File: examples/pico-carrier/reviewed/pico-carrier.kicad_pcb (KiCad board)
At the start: 2 copper layers, 88 x 62 mm, 9 parts, among them J1 5V IN, J3 GP0-GP15, J4 GP16-GP28, PWR, U1 Pico

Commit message: Keep vias out of the lands they would drain
The reviewer's next one, and it is not one board's problem: vias were
landing inside surface-mount lands across the set. A hole in a land is a
hole solder wicks down during reflow - the joint above it starves, and
nothing on the assembled board tells that apart from a cold one.
Via-in-pad is a real technique and a filled-and-capped process, not a
drawing; a layout that has not specified the process may not draw it.

The router was the source. `_blocked` skips a route's own net, so
nothing stopped a layer change from happening on the very land the route
started at, and eighteen vias across three boards sat in one. Pads are
now marked as pads in the obstacle list and every one of them, whoever
owns it, is a cell where a via may not go - so an escape that has to
reach the plane leaves the land first and turns its via beside it. The
stitching pass kept ground vias a via-radius from ground lands where it
kept signal ones a radius plus clearance; both are the same distance
now, because the plane gains nothing from touching a land it can reach a
stub away.

`via.in_pad` measures the copper gap from every via to every land and
reports what is left. The exposed thermal pad under a package is exempt
- the via array in one is the datasheet's own answer, and nothing a
signal reaches is four square millimetres. It blocks under the
ai-generated policy: a generated board has no reason to draw this.

The test fixture had one too, a via twenty-five microns into C1's ground
land; it moves three tenths of a millimetre and the board is DRC clean
on both matrix versions as before.

Co-Authored-By: Claude Fable 5 <noreply@anthropic.com>
Claude-Session: https://claude.ai/code/session_01DUj7Ltu92tWg159mCSacwY
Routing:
- net GND: track 65.7 -> 66.1 mm, vias 56 -> 55
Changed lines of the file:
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@@
 	(segment (start 135.69 94.48) (end 142.0 94.48) (width 0.8) (layer "F.Cu") (net 1))
 	(segment (start 135.69 107.18) (end 142.0 107.18) (width 0.8) (layer "F.Cu") (net 1))
-	(segment (start 152.0 67.045) (end 152.045 67.045) (width 0.5) (layer "F.Cu") (net 1))
-	(segment (start 152.045 67.045) (end 152.25 67.25) (width 0.5) (layer "F.Cu") (net 1))
-	(segment (start 152.25 67.25) (end 153.5 68.5) (width 0.5) (layer "F.Cu") (net 1))
-	(segment (start 153.5 68.5) (end 155.0 70.0) (width 0.5) (layer "B.Cu") (net 1))
-	(segment (start 155.0 70.0) (end 155.0 74.0) (width 0.5) (layer "B.Cu") (net 1))
+	(segment (start 152.0 67.045) (end 152.205 67.045) (width 0.5) (layer "F.Cu") (net 1))
+	(segment (start 152.205 67.045) (end 152.25 67.0) (width 0.5) (layer "F.Cu") (net 1))
+	(segment (start 152.25 67.0) (end 152.75 67.0) (width 0.5) (layer "F.Cu") (net 1))
+	(segment (start 152.75 67.0) (end 154.25 68.5) (width 0.5) (layer "F.Cu") (net 1))
+	(segment (start 154.25 68.5) (end 155.0 69.25) (width 0.5) (layer "B.Cu") (net 1))
+	(segment (start 155.0 69.25) (end 155.0 74.0) (width 0.5) (layer "B.Cu") (net 1))
 	(segment (start 152.95 77.0) (end 154.5 77.0) (width 0.5) (layer "F.Cu") (net 1))
 	(segment (start 170.9375 77.0) (end 171.0 77.0) (width 0.5) (layer "F.Cu") (net 1))
@@
 	(segment (start 159.5 75.5) (end 149.5 75.5) (width 0.4) (layer "F.Cu") (net 2))
 	(segment (start 162.9125 77.0) (end 169.0625 77.0) (width 0.3) (layer "F.Cu") (net 33))
-	(via (at 153.5 68.5) (size 0.8) (drill 0.4) (layers "F.Cu" "B.Cu") (net 1))
+	(via (at 154.25 68.5) (size 0.8) (drill 0.4) (layers "F.Cu" "B.Cu") (net 1))
 	(via (at 154.5 77.0) (size 0.8) (drill 0.4) (layers "F.Cu" "B.Cu") (net 1))
 	(via (at 174.0 81.0) (size 0.8) (drill 0.4) (layers "F.Cu" "B.Cu") (net 1))
@@
 	(via (at 102.7 112.7) (size 0.8) (drill 0.4) (layers "F.Cu" "B.Cu") (net 1))
 	(via (at 185.3 112.7) (size 0.8) (drill 0.4) (layers "F.Cu" "B.Cu") (net 1))
-	(via (at 108.7 68.7) (size 0.8) (drill 0.4) (layers "F.Cu" "B.Cu") (net 1))
 	(via (at 120.7 68.7) (size 0.8) (drill 0.4) (layers "F.Cu" "B.Cu") (net 1))
 	(via (at 156.7 68.7) (size 0.8) (drill 0.4) (layers "F.Cu" "B.Cu") (net 1))

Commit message: Give the vias room to stand beside the lands
Following the via-in-pad ban, the FPGA board stopped routing: five
attempts, five different nets, each one out of lanes in the corridor
between the FPGA's east escape fan and the codec's west one. Three
changes, in the order a layout would make them.

The via spacing was guesswork and is now the fab's. Hole to hole goes
from 1.2 mm to 0.9, which at the shipped 0.8/0.4 via leaves half a
millimetre of laminate between barrels - the ordinary minimum - and in a
1 mm-pitch escape comb is the difference between a lane and no lane.
What a via keeps off a land it may not sit in is its own radius plus a
solder-mask dam rather than the track clearance: the copper either side
may well be the same net, and what has to be true is that the mask can
part the barrel from the land.

Every decoupling capacitor now has its ground via placed against its own
pad rather than nine of them asking the search for one, and where the
via goes is chosen rather than fixed: `anchor_site` takes the nearest
position that clears everything already placed, fanning either side of
the direction facing off the part. A fixed offset walled off the
corridor its neighbour's supply needed - the via was legal, and it was
in the way.

And the seven parts sitting inside that corridor - four decoupling
capacitors, the two 1.2 V ones and the LED resistor - move four
millimetres south into the empty band below it. Twelve lanes leaving the
FPGA and ten arriving at the codec have eleven millimetres to cross in;
what a hand would do first is stop parking capacitors in the middle of
that, and it is the floorplan half of the debt this board's own README
has been carrying.

Co-Authored-By: Claude Fable 5 <noreply@anthropic.com>
Claude-Session: https://claude.ai/code/session_01DUj7Ltu92tWg159mCSacwY
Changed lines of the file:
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@@
 	(segment (start 135.69 94.48) (end 142.0 94.48) (width 0.8) (layer "F.Cu") (net 1))
 	(segment (start 135.69 107.18) (end 142.0 107.18) (width 0.8) (layer "F.Cu") (net 1))
-	(segment (start 152.0 67.045) (end 152.205 67.045) (width 0.5) (layer "F.Cu") (net 1))
-	(segment (start 152.205 67.045) (end 152.25 67.0) (width 0.5) (layer "F.Cu") (net 1))
-	(segment (start 152.25 67.0) (end 152.75 67.0) (width 0.5) (layer "F.Cu") (net 1))
-	(segment (start 152.75 67.0) (end 154.25 68.5) (width 0.5) (layer "F.Cu") (net 1))
-	(segment (start 154.25 68.5) (end 155.0 69.25) (width 0.5) (layer "B.Cu") (net 1))
-	(segment (start 155.0 69.25) (end 155.0 74.0) (width 0.5) (layer "B.Cu") (net 1))
+	(segment (start 152.0 67.045) (end 152.045 67.045) (width 0.5) (layer "F.Cu") (net 1))
+	(segment (start 152.045 67.045) (end 152.25 67.25) (width 0.5) (layer "F.Cu") (net 1))
+	(segment (start 152.25 67.25) (end 153.5 68.5) (width 0.5) (layer "F.Cu") (net 1))
+	(segment (start 153.5 68.5) (end 155.0 70.0) (width 0.5) (layer "B.Cu") (net 1))
+	(segment (start 155.0 70.0) (end 155.0 74.0) (width 0.5) (layer "B.Cu") (net 1))
 	(segment (start 152.95 77.0) (end 154.5 77.0) (width 0.5) (layer "F.Cu") (net 1))
 	(segment (start 170.9375 77.0) (end 171.0 77.0) (width 0.5) (layer "F.Cu") (net 1))
@@
 	(segment (start 159.5 75.5) (end 149.5 75.5) (width 0.4) (layer "F.Cu") (net 2))
 	(segment (start 162.9125 77.0) (end 169.0625 77.0) (width 0.3) (layer "F.Cu") (net 33))
-	(via (at 154.25 68.5) (size 0.8) (drill 0.4) (layers "F.Cu" "B.Cu") (net 1))
+	(via (at 153.5 68.5) (size 0.8) (drill 0.4) (layers "F.Cu" "B.Cu") (net 1))
 	(via (at 154.5 77.0) (size 0.8) (drill 0.4) (layers "F.Cu" "B.Cu") (net 1))
 	(via (at 174.0 81.0) (size 0.8) (drill 0.4) (layers "F.Cu" "B.Cu") (net 1))

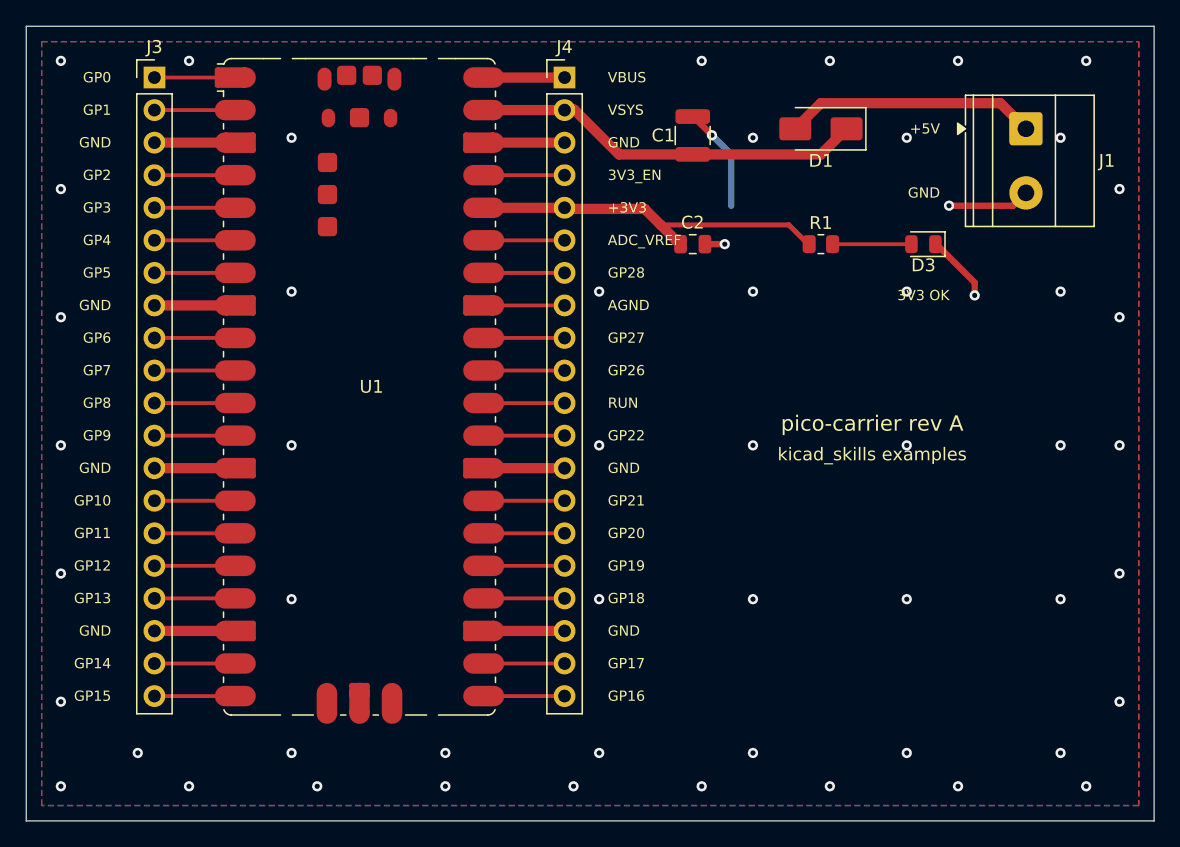
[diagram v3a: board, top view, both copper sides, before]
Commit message: Relieve the pads, fillet the joints, and give the board its screw holes
Three of the reviewer's manufacturing points, and they largely fall out
of the one before it - once KiCad fills the plane, the thermal relief it
was already asked for in the file actually appears.

**Thermal relief.** The zones said thermal all along; our own filler
ignored it and flooded every land solid. KiCad's does not, so every
through-hole ground pad now sits in a gap bridged by four spokes and an
iron can bring the joint up without heating a hundred square millimetres
of copper. `layout.solid_pad_connection` reports the setting when a
board turns it off: drilled pads only, because a surface pad reflows in
an oven that is heating the plane anyway and flooding it is often the
better thermal answer.

**Teardrops.** A track entering a land is a step change in width, and a
step change is where copper tears - the connector gets levered on and
off, the drill wanders, and the crack starts at the corner. `_teardrops`
replaces the first stretch of each run with a three-step taper into the
land, checked against its neighbours before it is kept, so a fillet
never eats the clearance a fine-pitch escape needs. It *replaces* rather
than overlays: laying the taper on top of the run drew the same copper
twice, and `route.acute_angle` reported all thirty of them, correctly.
`route.mixed_track_widths` learns what a fillet looks like so a properly
filleted board does not read as one nobody decided the width of.

**Mounting holes.** Four M3 holes near the corners, placed before the
router runs because they are obstacles, and slid along the edges or a
little inboard where a connector body has the corner - the motor board
and the op-amp take three, which is what those floorplans have room for.
Grounded on the motor driver, whose chassis is metal and part of the
shield, plain on the rest: bonding the enclosure to the reference is the
enclosure's decision, not the board's.

Two things that fell out of placing par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
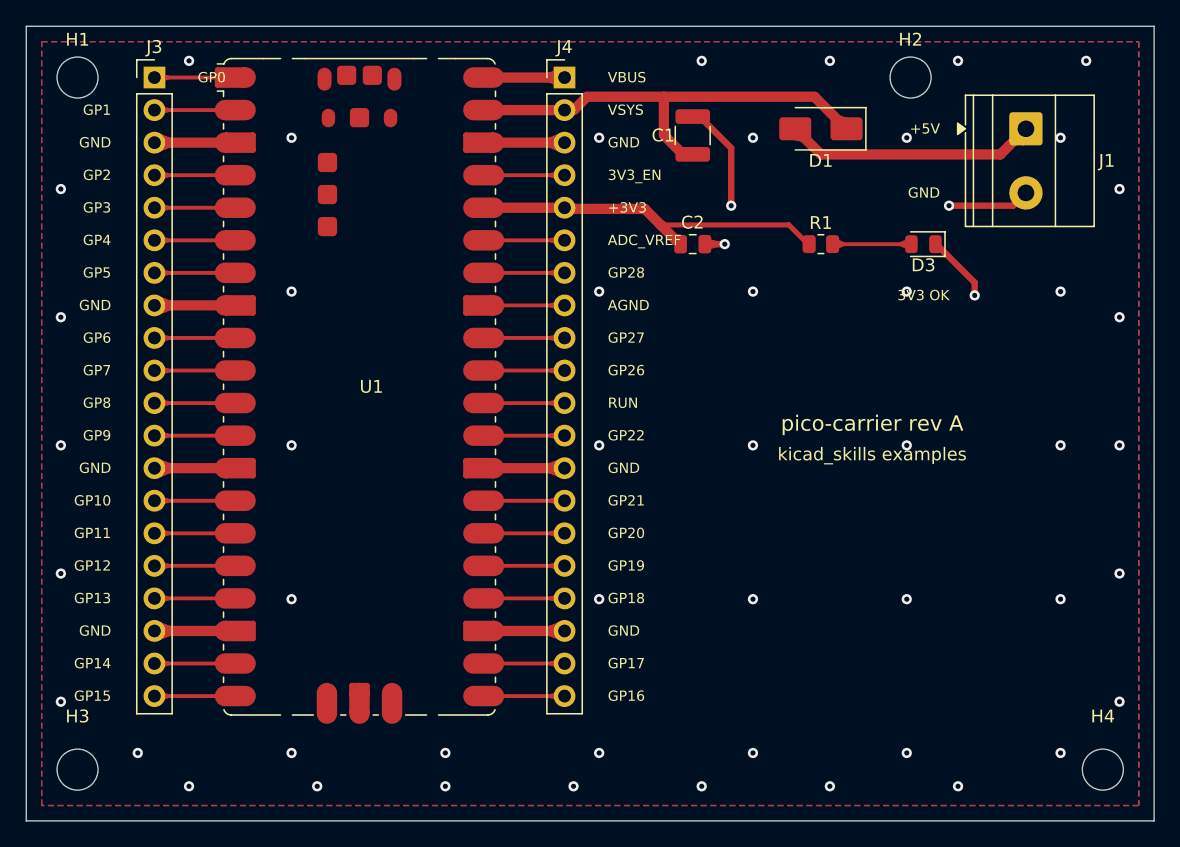
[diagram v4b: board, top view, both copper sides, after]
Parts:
- added H1: M33, MountingHole:MountingHole_3.2mm_M3, F.Cu at (104.0, 64.0)
- added H2: M33, MountingHole:MountingHole_3.2mm_M3, F.Cu at (169.0, 64.0)
- added H3: M33, MountingHole:MountingHole_3.2mm_M3, F.Cu at (104.0, 118.0)
- added H4: M33, MountingHole:MountingHole_3.2mm_M3, F.Cu at (184.0, 118.0)
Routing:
- net /VSYS: track 30.6 -> 35.6 mm
- net GND: track 65.7 -> 66.0 mm, vias 55 -> 53

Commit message: Give the assembly machine something to aim at
Fiducials: three copper dots in bare mask windows, near three different
corners so a pick-and-place gets rotation as well as offset. It aligns
to the board, not to the drawing - without them it has only the routed
outline, cut to a tolerance ten times looser than the placement a 0.5 mm
pitch part is asking for. `fab.no_fiducials` reports a fine-pitch board
that has none, as context rather than as a fault: plenty of boards are
built one at a time with tweezers.

They share the corner search with the mounting holes, which is where
this found a real bug: `_courtyard_box` read lines and rectangles only,
and a mounting hole draws its courtyard as one circle - so every hole
measured as taking up no room at all, and the first three fiducials
landed on top of three screw holes. Circles and arcs count now.

Co-Authored-By: Claude Fable 5 <noreply@anthropic.com>
Claude-Session: https://claude.ai/code/session_01DUj7Ltu92tWg159mCSacwY
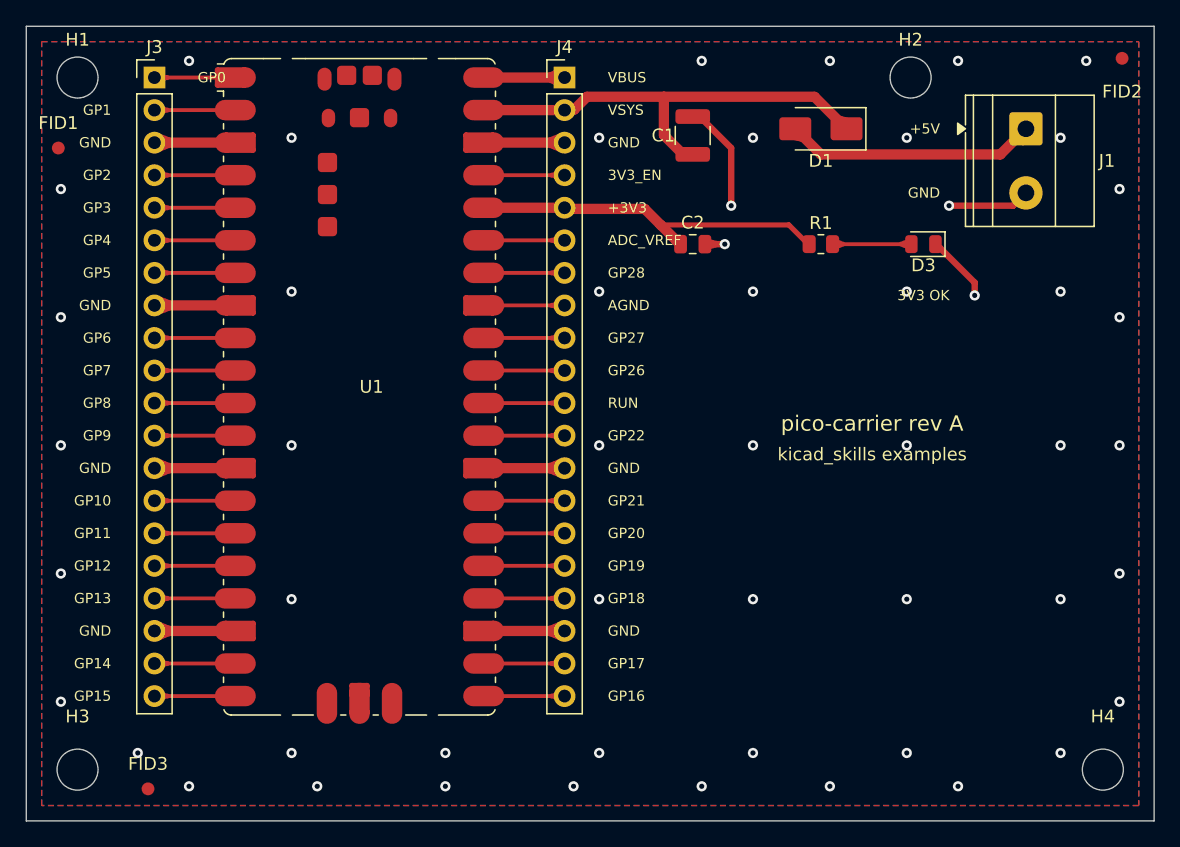
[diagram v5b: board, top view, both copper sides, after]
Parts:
- added FID1: Fiducial, Fiducial:Fiducial_1mm_Mask2mm, F.Cu at (102.5, 69.5)
- added FID2: Fiducial, Fiducial:Fiducial_1mm_Mask2mm, F.Cu at (185.5, 62.5)
- added FID3: Fiducial, Fiducial:Fiducial_1mm_Mask2mm, F.Cu at (109.5, 119.5)
- H1, H2, H3, H4: value M33 -> M3
